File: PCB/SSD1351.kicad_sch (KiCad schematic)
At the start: 20 parts, among them J1 Conn_01x07, U1 SFV30R-4STBE1HLF, U2 FAN5331SXCT-ND

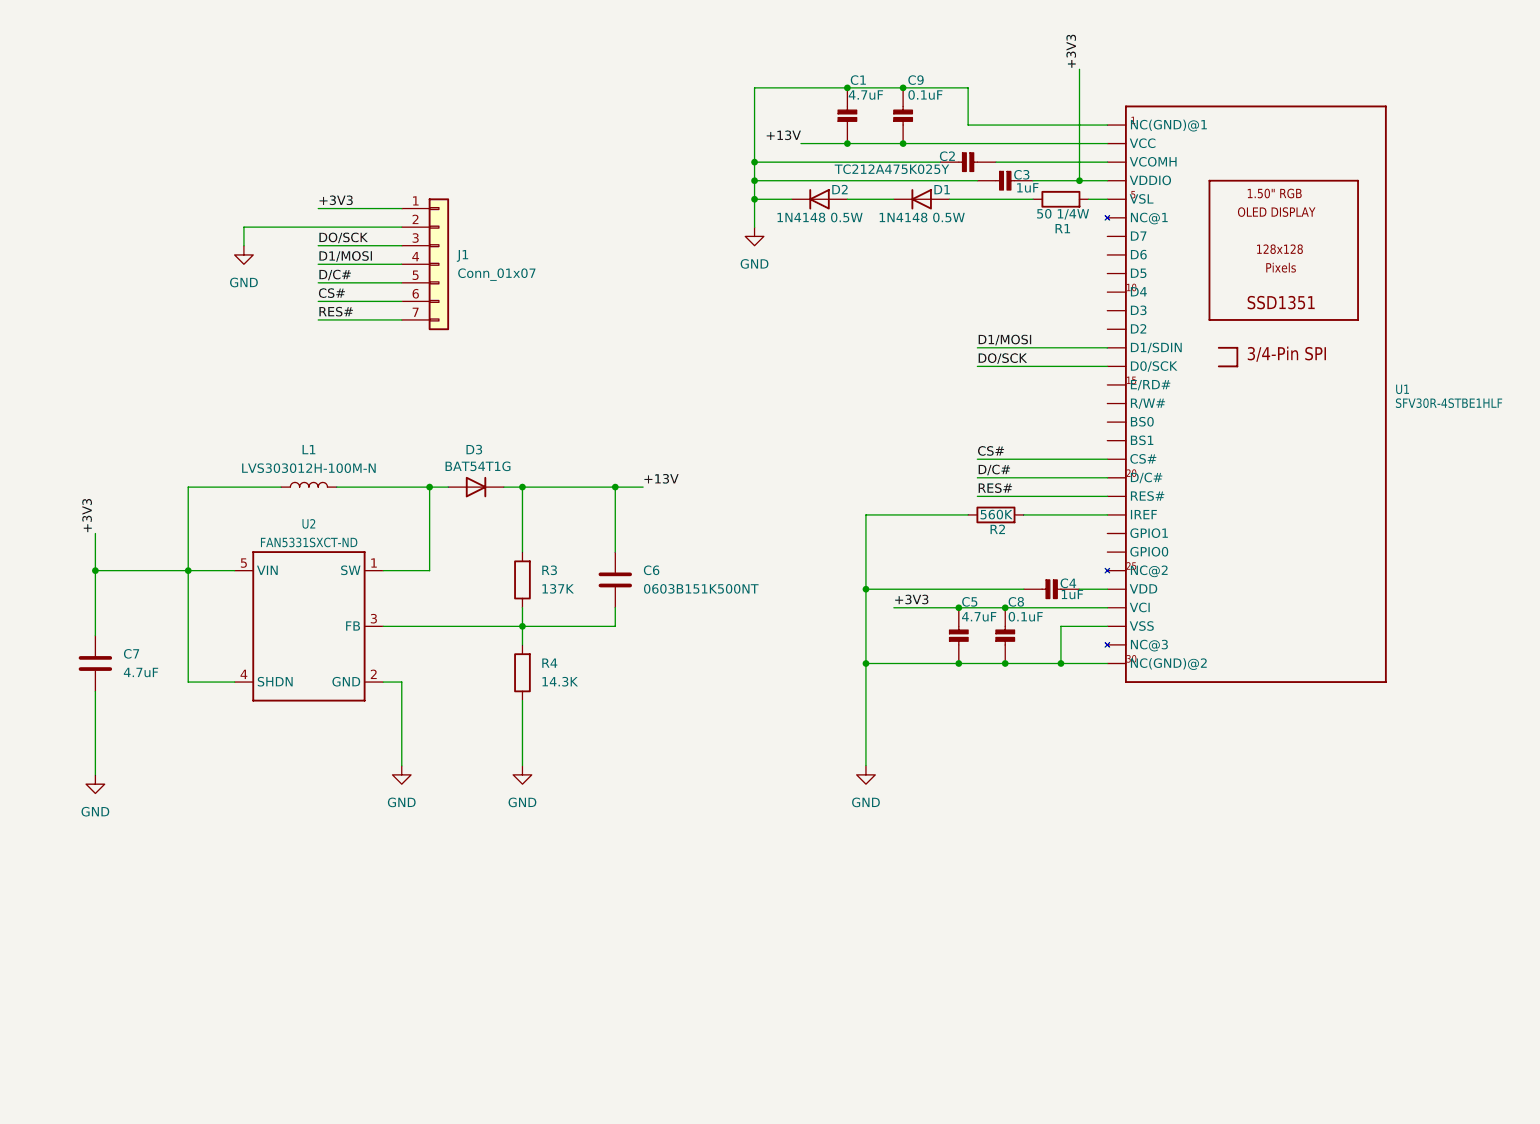
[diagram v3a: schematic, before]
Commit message: Adding datasheets and more pcb design changes
* Added datasheets for ICs
* Removed unused footprints
* Updated PCB to use correct sized caps
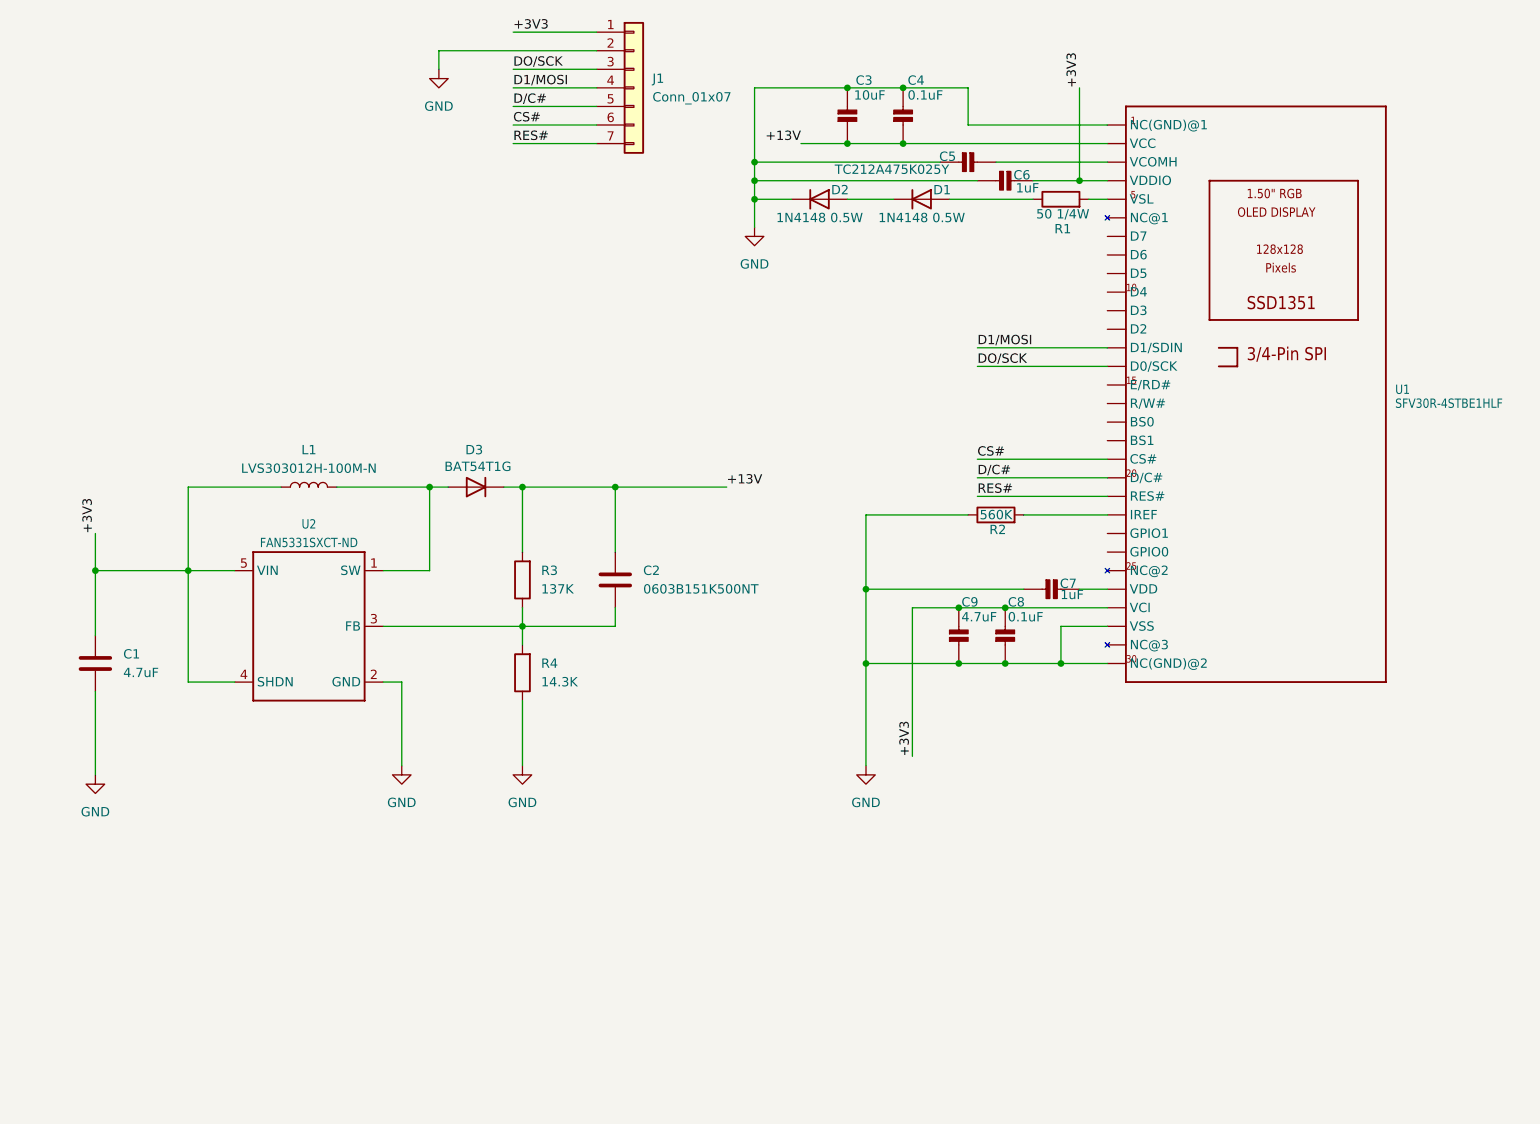
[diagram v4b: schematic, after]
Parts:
- removed C1: 4.7uF, Capacitor_SMD:C_0805_2012Metric, symbol SSD1351:CAP_CERAMIC_0805
- added C3: 10uF, Capacitor_SMD:C_1206_3216Metric, symbol SSD1351:CAP_CERAMIC_0805
- C6: renamed from C3; footprint Capacitor_SMD:C_0603_1608Metric -> Capacitor_SMD:C_0805_2012Metric
- C7: renamed from C4; footprint Capacitor_SMD:C_0603_1608Metric -> Capacitor_SMD:C_0805_2012Metric
- renumbered C7 to C1, C6 to C2, C9 to C4, C2 to C5, C5 to C9
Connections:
- net +13V: now also C3.2 (P$2)
- net GND: now also C3.1 (P$1)
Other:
- moved on the sheet: J1

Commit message: Changing 13v boost converter
Replace the FAN5331 with MIC2288 as a result of some sourcing issues. Redesigned and updated all the relevant components.

Added in some new footprints to make hand soldering easier for inductor and boost converter.
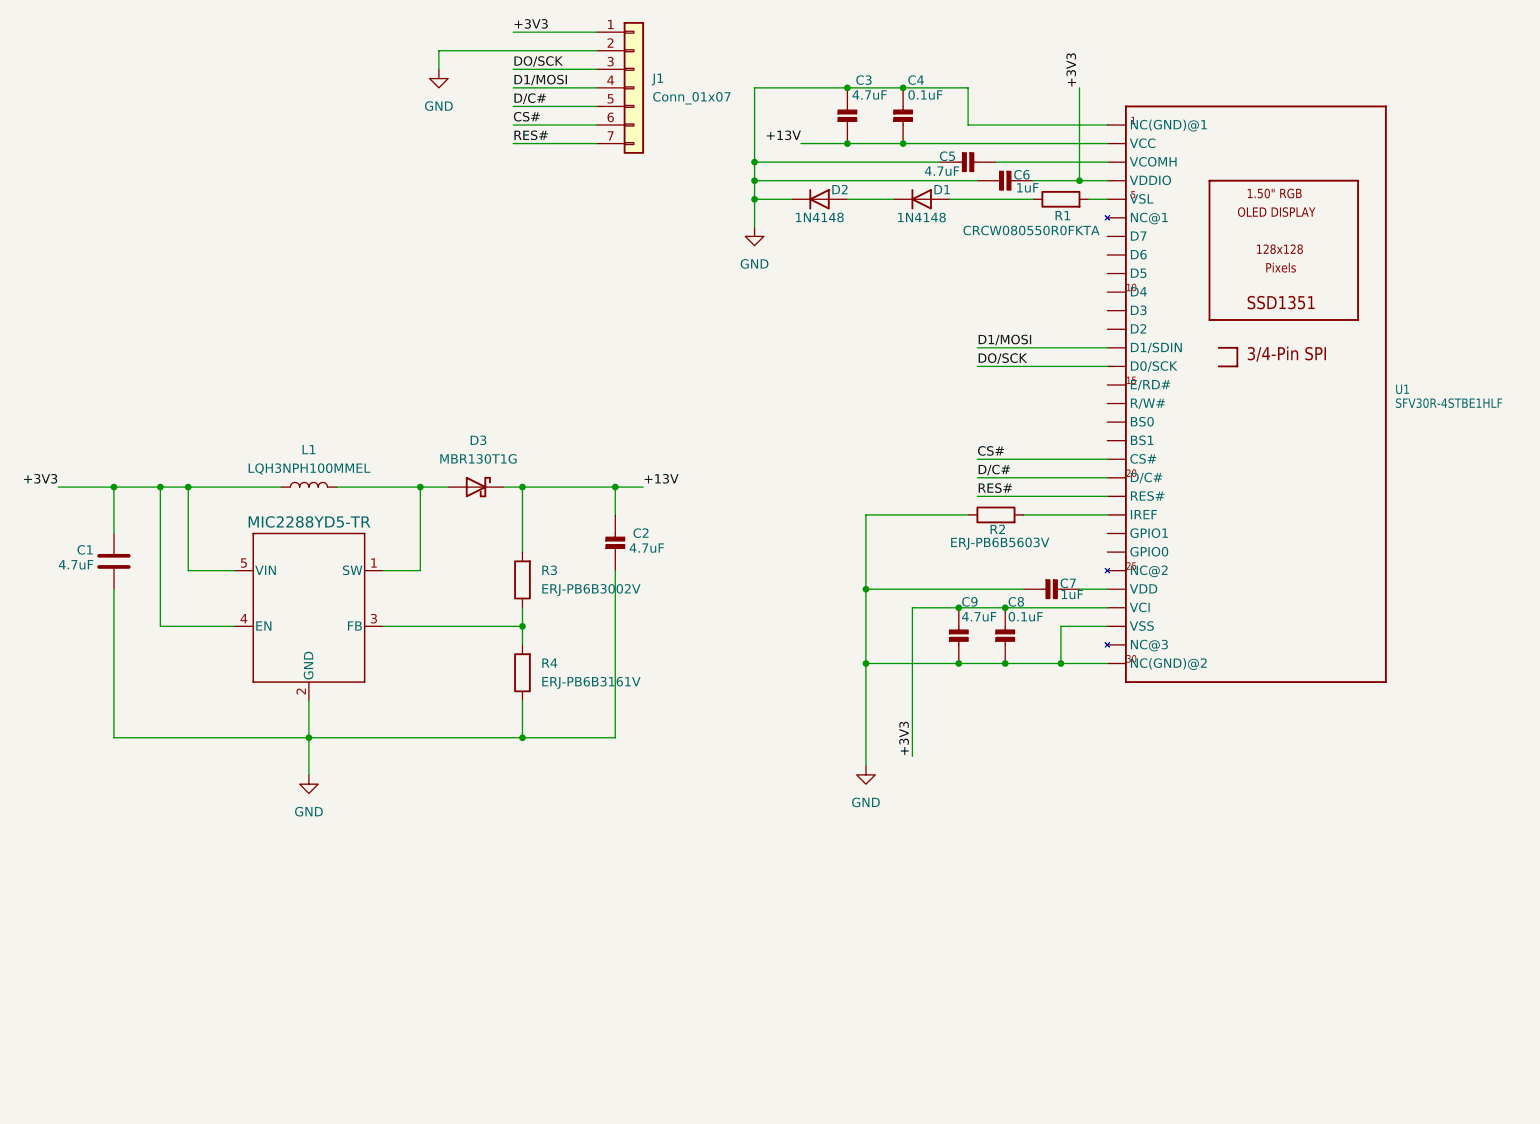
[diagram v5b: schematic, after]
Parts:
- removed C2: 0603B151K500NT, Capacitor_SMD:C_0603_1608Metric, symbol Device:C
- removed D3: BAT54T1G, Diode_SMD:D_SOD-123, symbol Device:D
- removed U2: FAN5331SXCT-ND, Package_TO_SOT_SMD:SOT-23-5_HandSoldering, symbol SSD1351:FAN5331
- added C2: 4.7uF, Capacitor_SMD:C_1206_3216Metric, symbol SSD1351:CAP_CERAMIC_0805
- added D3: MBR130T1G, Diode_SMD:D_SOD-123, symbol Device:D_Schottky
- added U2: MIC2288YD5-TR, SSD1351:TSOT-23-5_D5_MCH, symbol MIC2288YD5-TR:MIC2288YD5-TR
- C3: value 10uF -> 4.7uF
- C5: value TC212A475K025Y -> 4.7uF; footprint Capacitor_Tantalum_SMD:CP_EIA-3216-18_Kemet-A -> Capacitor_SMD:C_1206_3216Metric
- D1, D2: value 1N4148 0.5W -> 1N4148
- L1: value LVS303012H-100M-N -> LQH3NPH100MMEL; footprint Inductor_SMD:L_Sunlord_SWPA3012S -> SSD1351:IND_LQH3NPH100MMEL
- R1: value 50 1/4W -> CRCW080550R0FKTA
- R2: value 560K -> ERJ-PB6B5603V
- R3: value 137K -> ERJ-PB6B3002V
- R4: value 14.3K -> ERJ-PB6B3161V
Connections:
- net +13V: now also C2.1 (P$1), D3.1 (K)
- net +3V3: now also U2.4 (EN), U2.5 (VIN)
- net GND: now also C2.2 (P$2), U2.2 (GND)
- net at L1.2: now also D3.2 (A), U2.1 (SW)
- net at R3.1, R4.2: now also U2.3 (FB)
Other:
- moved on the sheet: C1

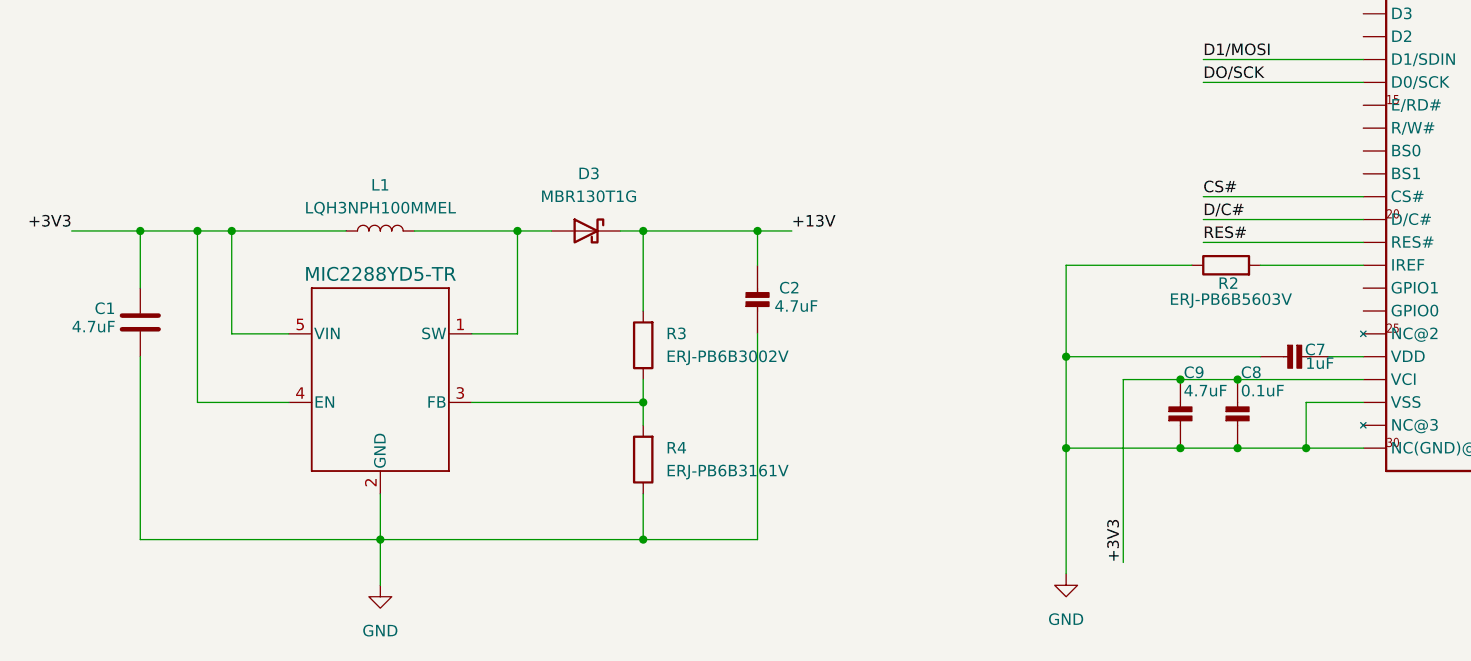
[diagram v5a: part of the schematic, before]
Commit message: More power system changes
Swapping out MLC2288 for TLV61046A and removing redundant diode.

Also swapped out inductor for a more efficient one.
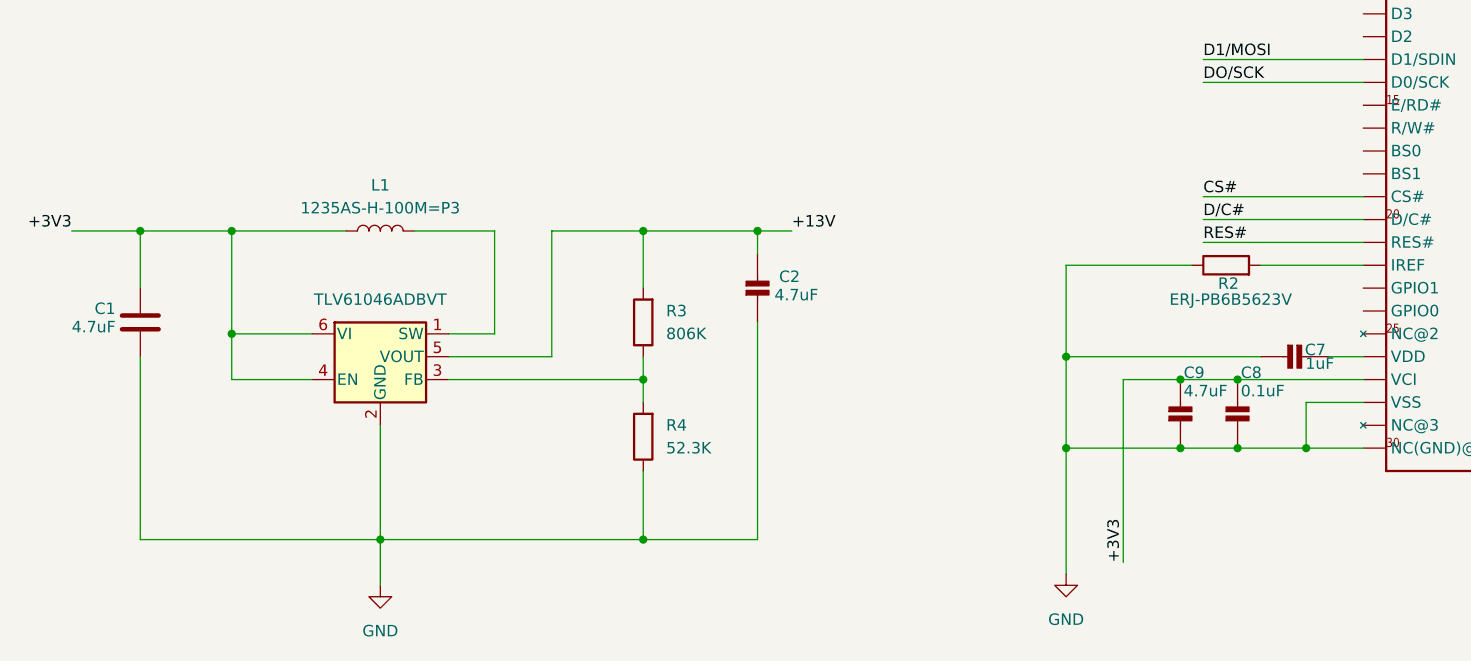
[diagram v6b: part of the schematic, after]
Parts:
- removed D3: MBR130T1G, Diode_SMD:D_SOD-123, symbol Device:D_Schottky
- removed U2: MIC2288YD5-TR, SSD1351:TSOT-23-5_D5_MCH, symbol MIC2288YD5-TR:MIC2288YD5-TR
- added U2: TLV61046ADBVT, Package_TO_SOT_SMD:SOT-23-6, symbol Regulator_Switching:TLV61046ADB
- L1: value LQH3NPH100MMEL -> 1235AS-H-100M=P3; footprint SSD1351:IND_LQH3NPH100MMEL -> SSD1351:IND_1235AS-H-100M=P3
- R2: value ERJ-PB6B5603V -> ERJ-PB6B5623V
- R3: value ERJ-PB6B3002V -> 806K
- R4: value ERJ-PB6B3161V -> 52.3K
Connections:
- net +13V: now also U2.5 (VOUT)
- net +3V3: now also U2.4 (EN), U2.6 (VI)
- net GND: now also U2.2 (GND)
- net at L1.2: now also U2.1 (SW)
- net at R3.1, R4.2: now also U2.3 (FB)
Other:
- moved on the sheet: C2, R3, R4
